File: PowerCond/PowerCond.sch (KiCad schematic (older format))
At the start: 42 parts, among them J1 Conn_01x02, J10 Conn_01x01, J11 Conn_01x01, J12 Conn_01x01, J2 Conn_01x02, J3 Conn_01x02, J4 Conn_01x02, J5 Conn_01x02, J6 Conn_01x02, J7 Conn_01x02, J8 Conn_01x02, J9 Conn_01x01, T1 Transformer_1P1Sdotted, T2 Transformer_1P1Sdotted, T3 Transformer_1P1Sdotted, T4 Transformer_1P1Sdotted

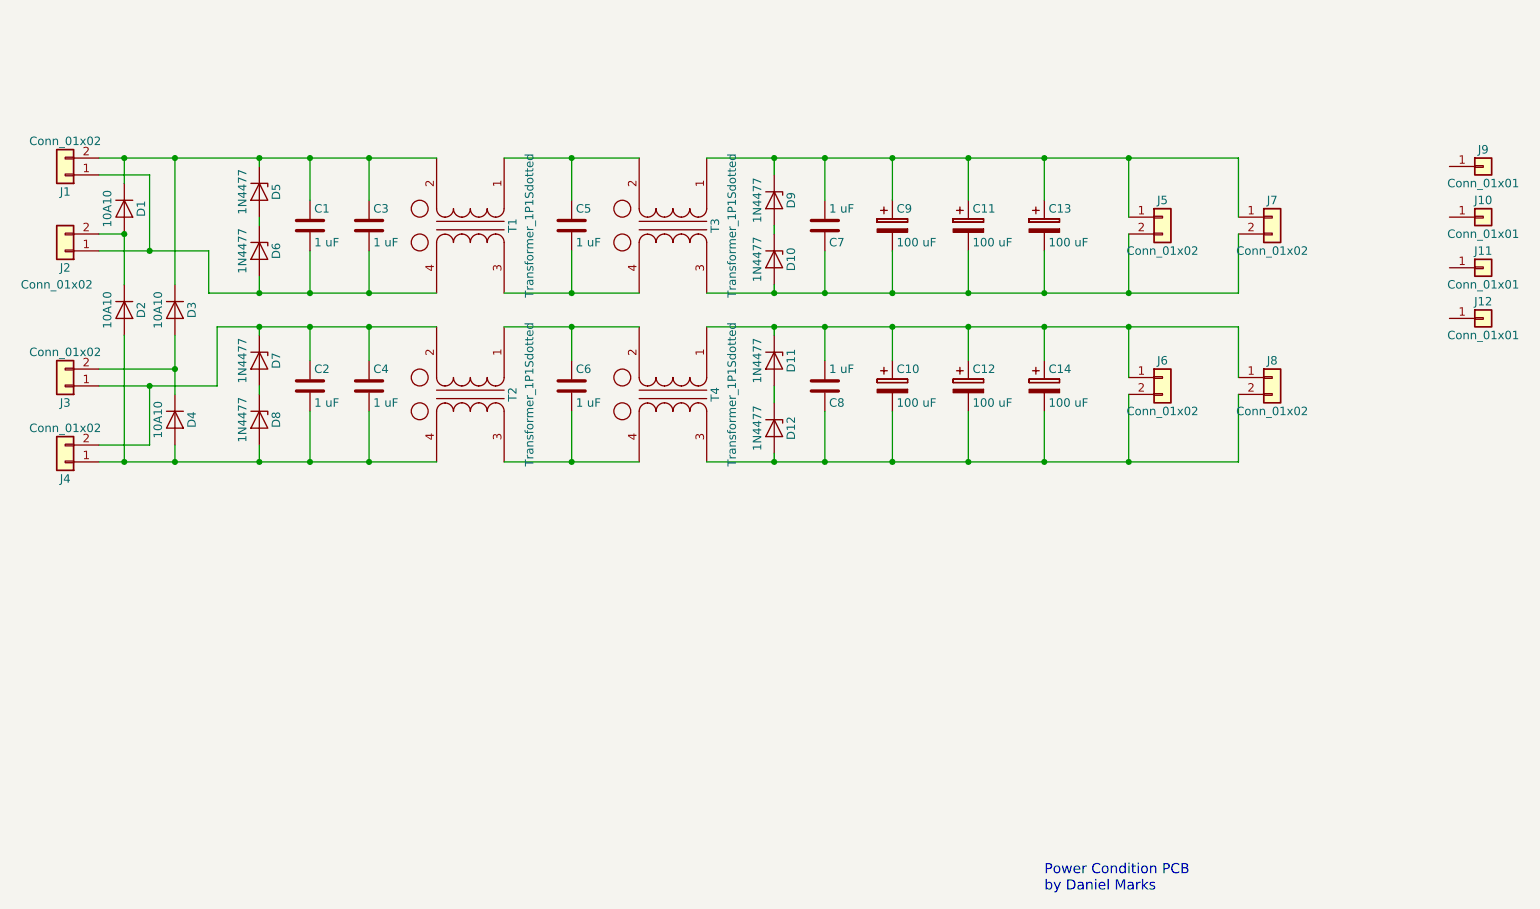
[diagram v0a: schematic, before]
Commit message: Added XLRtoBal
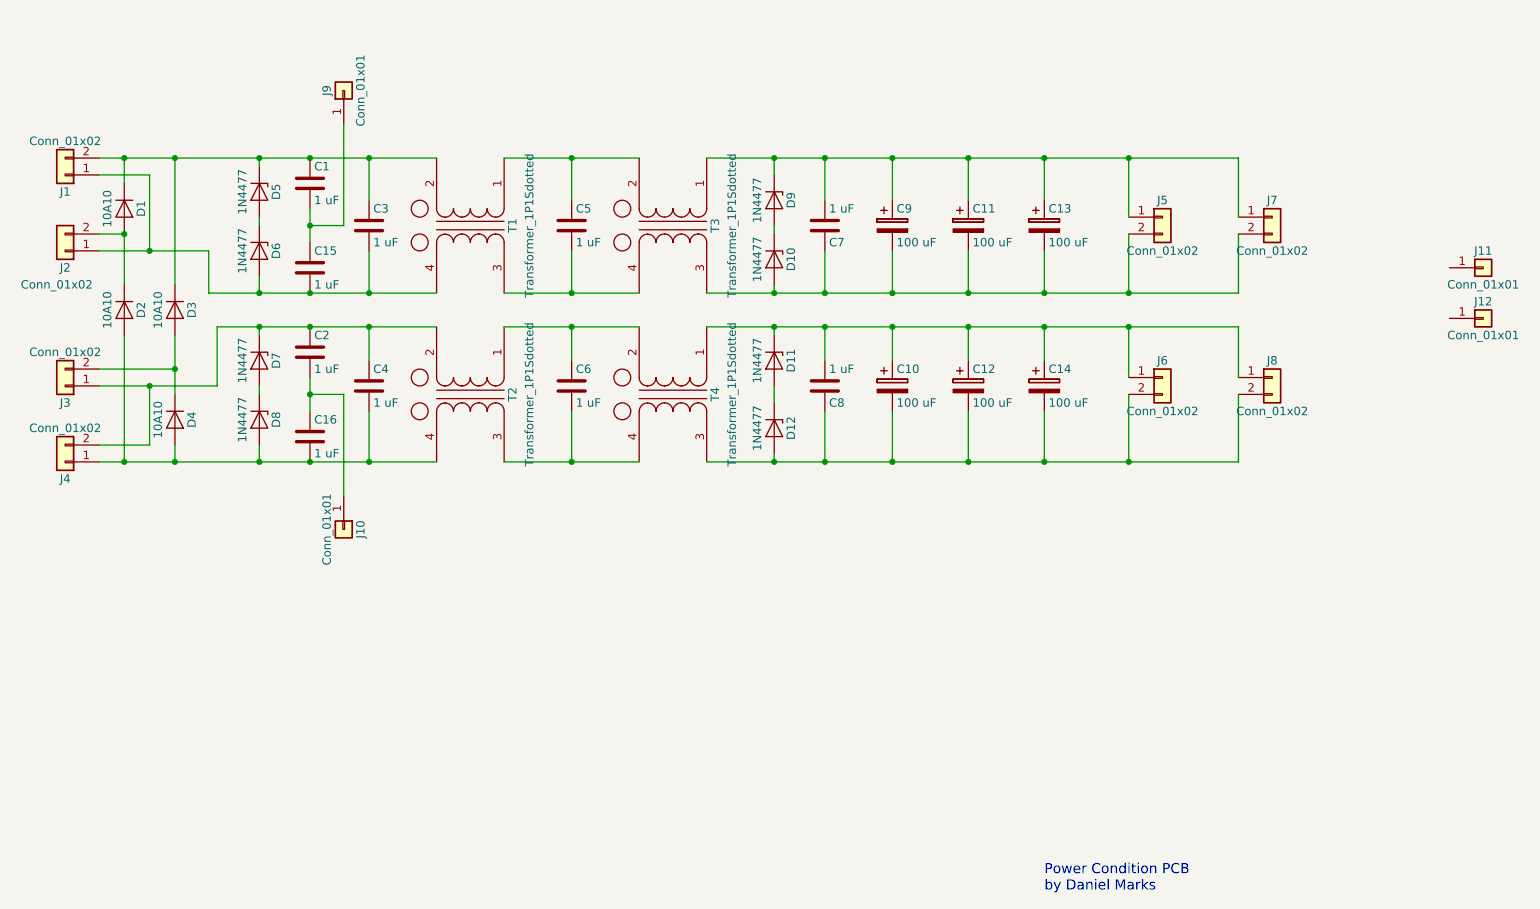
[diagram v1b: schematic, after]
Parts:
- added C15, C16: 1 uF, Capacitors_THT:C_Axial_L5.1mm_D3.1mm_P12.50mm_Horizontal, symbol C
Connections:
- net at J9.1 (Pin_1): now also C1.2, C15.1
- net at J10.1 (Pin_1): now also C2.2, C16.1
- net at C3.2, D6.2 (A), J1.1 (Pin_1)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: now also C15.2; no longer C1.2
- net at C4.2, D2.2 (A), D4.2 (A)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: now also C16.2; no longer C2.2
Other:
- moved on the sheet: C1, C2, J10, J9
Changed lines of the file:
@@
 L C C1
 U 1 1 5F3E50C0
-P 3200 3000
-F 0 "C1" H 3225 3100 50  0000 L CNN
-F 1 "1 uF" H 3225 2900 50  0000 L CNN
-F 2 "Capacitors_THT:C_Axial_L5.1mm_D3.1mm_P12.50mm_Horizontal" H 3238 2850 50  0001 C CNN
-F 3 "" H 3200 3000 50  0001 C CNN
-	1    3200 3000
-	1    0    0    -1
-$EndComp
-Wire Wire Line
-	3200 2850 3200 2600
+P 3200 2750
+F 0 "C1" H 3225 2850 50  0000 L CNN
+F 1 "1 uF" H 3225 2650 50  0000 L CNN
+F 2 "Capacitors_THT:C_Axial_L5.1mm_D3.1mm_P12.50mm_Horizontal" H 3238 2600 50  0001 C CNN
+F 3 "" H 3200 2750 50  0001 C CNN
+	1    3200 2750
+	1    0    0    -1
+$EndComp
+Wire Wire Line
+	3200 2600 3200 2600
 Connection ~ 3200 2600
-Wire Wire Line
-	3200 3150 3200 3400
 Connection ~ 3200 3400
 $Comp
@@
 L C C2
 U 1 1 5F3E52BA
-P 3200 3950
-F 0 "C2" H 3225 4050 50  0000 L CNN
-F 1 "1 uF" H 3225 3850 50  0000 L CNN
-F 2 "Capacitors_THT:C_Axial_L5.1mm_D3.1mm_P12.50mm_Horizontal" H 3238 3800 50  0001 C CNN
-F 3 "" H 3200 3950 50  0001 C CNN
-	1    3200 3950
-	1    0    0    -1
-$EndComp
-Wire Wire Line
-	3200 3800 3200 3600
+P 3200 3750
+F 0 "C2" H 3225 3850 50  0000 L CNN
+F 1 "1 uF" H 3225 3650 50  0000 L CNN
+F 2 "Capacitors_THT:C_Axial_L5.1mm_D3.1mm_P12.50mm_Horizontal" H 3238 3600 50  0001 C CNN
+F 3 "" H 3200 3750 50  0001 C CNN
+	1    3200 3750
+	1    0    0    -1
+$EndComp
+Wire Wire Line
+	3200 3600 3200 3600
 Connection ~ 3200 3600
-Wire Wire Line
-	3200 4100 3200 4400
 Connection ~ 3200 4400
 $Comp
@@
 L Conn_01x01 J9
 U 1 1 5F3C25A0
-P 10150 2650
-F 0 "J9" H 10150 2750 50  0000 C CNN
-F 1 "Conn_01x01" H 10150 2550 50  0000 C CNN
-F 2 "Connectors:1pin" H 10150 2650 50  0001 C CNN
-F 3 "" H 10150 2650 50  0001 C CNN
-	1    10150 2650
-	1    0    0    -1
+P 3400 2200
+F 0 "J9" H 3400 2300 50  0000 C CNN
+F 1 "Conn_01x01" H 3400 2100 50  0000 C CNN
+F 2 "Connectors:1pin" H 3400 2200 50  0001 C CNN
+F 3 "" H 3400 2200 50  0001 C CNN
+	1    3400 2200
+	0    -1   -1   0
 $EndComp
 $Comp
 L Conn_01x01 J10
 U 1 1 5F3C2707
-P 10150 2950
-F 0 "J10" H 10150 3050 50  0000 C CNN
-F 1 "Conn_01x01" H 10150 2850 50  0000 C CNN
-F 2 "Connectors:1pin" H 10150 2950 50  0001 C CNN
-F 3 "" H 10150 2950 50  0001 C CNN
-	1    10150 2950
-	1    0    0    -1
+P 3400 4800
+F 0 "J10" H 3400 4900 50  0000 C CNN
+F 1 "Conn_01x01" H 3400 4700 50  0000 C CNN
+F 2 "Connectors:1pin" H 3400 4800 50  0001 C CNN
+F 3 "" H 3400 4800 50  0001 C CNN
+	1    3400 4800
+	0    1    1    0
 $EndComp
 $Comp
@@
 	1    0    0    -1
 $EndComp
+$Comp
+L C C15
+U 1 1 5F3CBB39
+P 3200 3250
+F 0 "C15" H 3225 3350 50  0000 L CNN
+F 1 "1 uF" H 3225 3150 50  0000 L CNN
+F 2 "Capacitors_THT:C_Axial_L5.1mm_D3.1mm_P12.50mm_Horizontal" H 3238 3100 50  0001 C CNN
+F 3 "" H 3200 3250 50  0001 C CNN
+	1    3200 3250
+	1    0    0    -1
+$EndComp
+Wire Wire Line
+	3200 3100 3200 2900
+$Comp
+L C C16
+U 1 1 5F3CBDE8
+P 3200 4250
+F 0 "C16" H 3225 4350 50  0000 L CNN
+F 1 "1 uF" H 3225 4150 50  0000 L CNN
+F 2 "Capacitors_THT:C_Axial_L5.1mm_D3.1mm_P12.50mm_Horizontal" H 3238 4100 50  0001 C CNN
+F 3 "" H 3200 4250 50  0001 C CNN
+	1    3200 4250
+	1    0    0    -1
+$EndComp
+Wire Wire Line
+	3200 4100 3200 3900
+Wire Wire Line
+	3400 2400 3400 3000
+Wire Wire Line
+	3400 3000 3200 3000
+Connection ~ 3200 3000
+Wire Wire Line
+	3400 4600 3400 4000
+Wire Wire Line
+	3400 4000 3200 4000
+Connection ~ 3200 4000
 $EndSCHEMATC

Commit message: Added soft start circuit
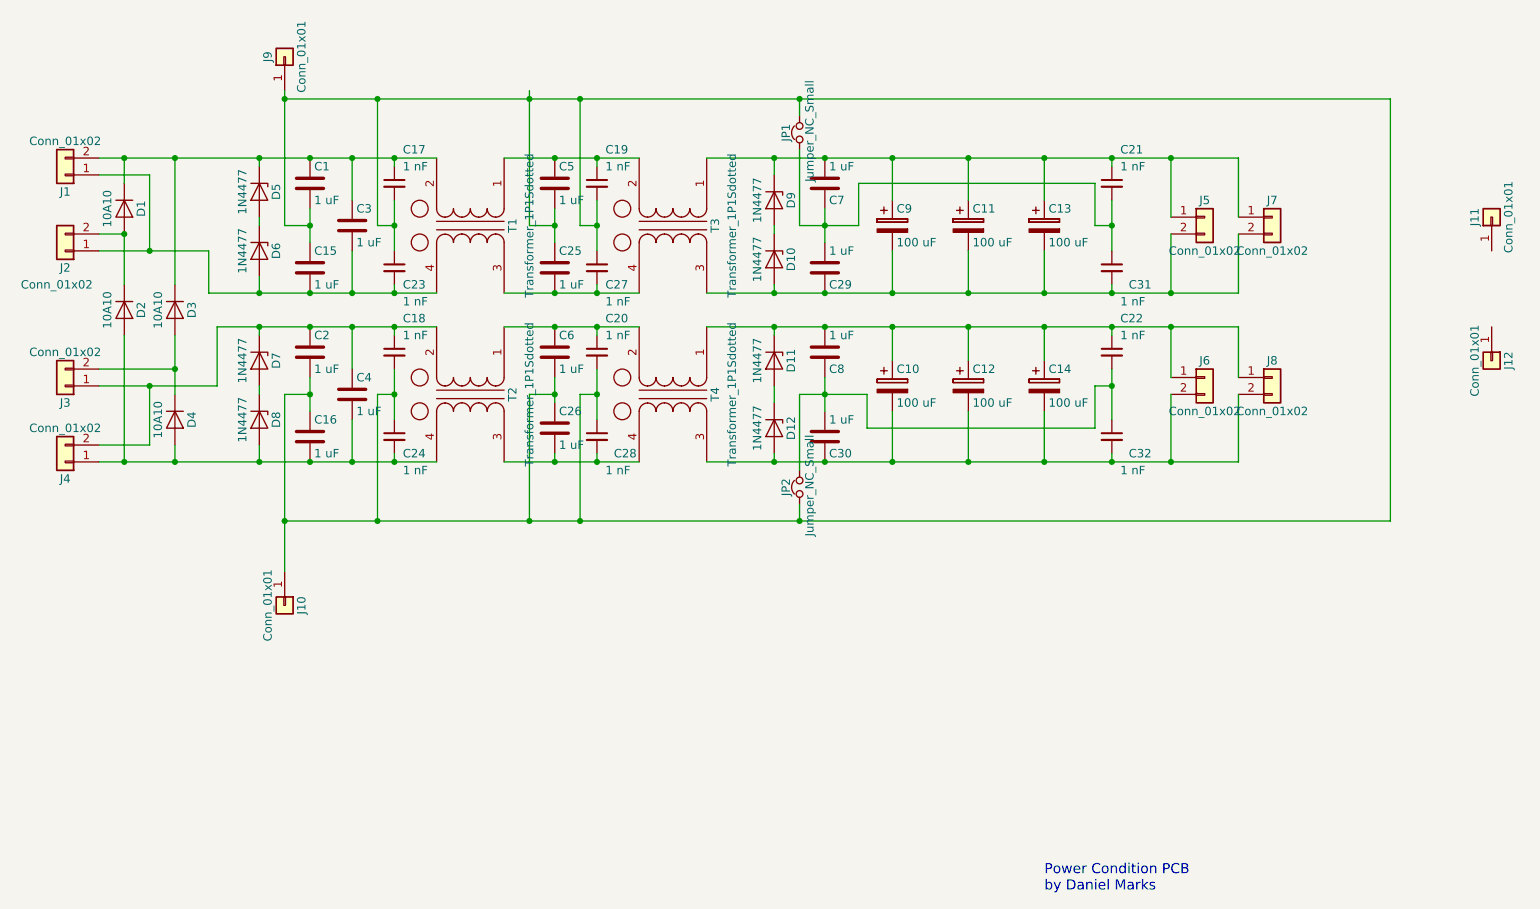
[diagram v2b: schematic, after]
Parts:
- added C17, C18, C19, C20, C21, C22, C23, C24, C27, C28, C31, C32: 1 nF, Capacitors_THT:C_Disc_D5.0mm_W2.5mm_P5.00mm, symbol C_Small
- added C25, C26, C29, C30: 1 uF, Capacitors_THT:C_Axial_L5.1mm_D3.1mm_P12.50mm_Horizontal, symbol C
- added JP1, JP2: Jumper_NC_Small, Pin_Headers:Pin_Header_Straight_1x02_Pitch2.54mm, symbol Jumper_NC_Small
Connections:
- net at C1.2, C15.1, J9.1 (Pin_1): now also C16.1, C2.2, C5.2, C6.2, J10.1 (Pin_1), C17.2, C18.2, C19.2, C20.2, C23.1, C24.1, C25.1, C26.1, C27.1, C28.1, JP1.2, JP2.1
- net at C15.2, C3.2, D6.2 (A)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: now also C23.2
- net at C16.2, C4.2, D2.2 (A)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: now also C24.2
- net at C5.1, T1.1 (AA), T3.2 (AB): now also C19.1
- net at C1.1, C3.1, D1.1 (K)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: now also C17.1
- net at T1.3 (SA), T3.4 (SB): now also C25.2, C27.2; no longer C5.2
- net at C2.1, C4.1, D7.1 (K)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: now also C18.1
- net at C6.1, T2.1 (AA), T4.2 (AB): now also C20.1
- net at T2.3 (SA), T4.4 (SB): now also C26.2, C28.2; no longer C6.2
- net at C11.1, C13.1, C7.2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: now also C21.1
- net at C11.2, C13.2, C9.2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: now also C29.1, C31.2; no longer C7.1
- net at C10.1, C12.1, C14.1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: now also C22.1
- net at C10.2, C12.2, C14.2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: now also C30.1, C32.2; no longer C8.1
- new net: C21.2, C29.2, C31.1, C7.1, JP1.1
- new net: C22.2, C30.2, C32.1, C8.1, JP2.2
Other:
- moved on the sheet: C3, C4, C5, C6, C7, C8, J10, J11, J12, J5, J6, J9

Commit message: Submitted to JLCPCB 2020-08-24
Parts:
- C1, C15, C16, C2, C25, C26, C29, C3, C30, C4, C5, C6, C7, C8: LCSC (none) -> C178471
- C10, C11, C12, C13, C14, C9: LCSC (none) -> C330940
- C17, C18, C20, C21, C22, C23, C24, C27, C28, C31, C32, T3: LCSC (none) -> C249151
- D1, D2, D3, D4: LCSC (none) -> C106904
- D10, D11, D12, D5, D6, D7, D8, D9: value 1N4477 -> 1N4755A; LCSC (none) -> C8043
- J1, J2, J3, J4, J5, J6, J7, J8: LCSC (none) -> C395849

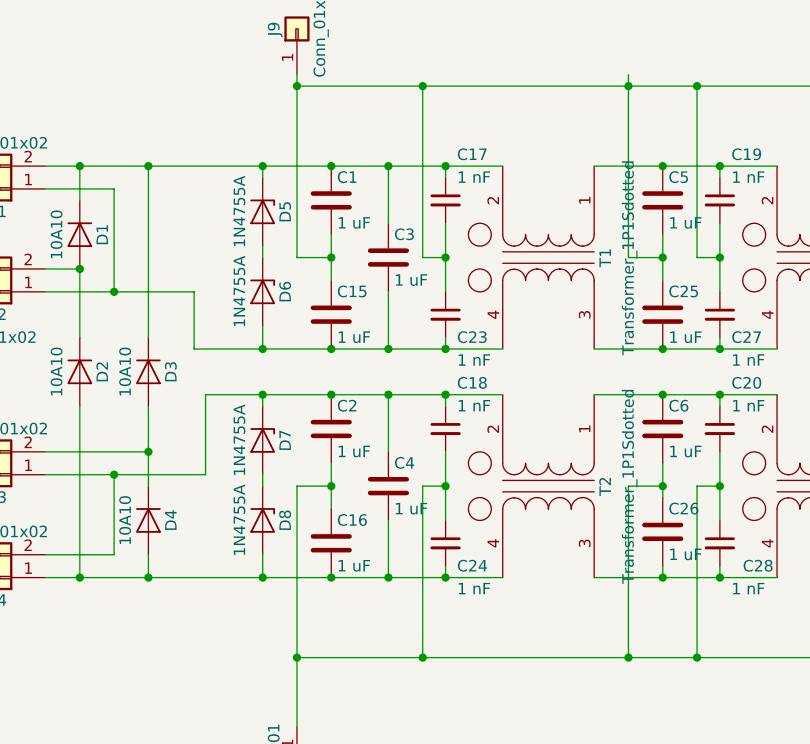
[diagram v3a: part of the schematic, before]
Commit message: Changed softstart and Poweramp to TO-220 transistors
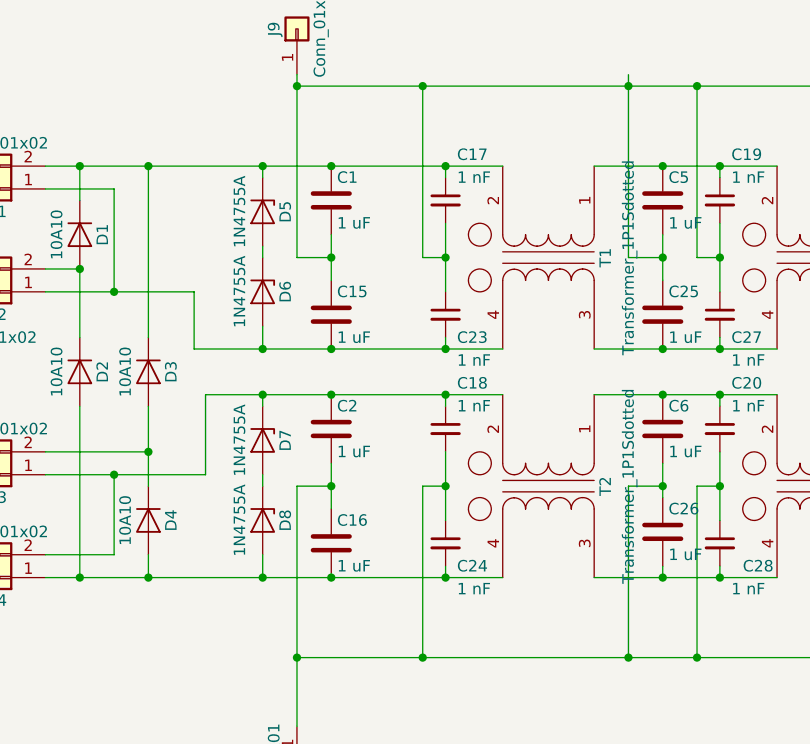
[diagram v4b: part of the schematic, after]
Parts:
- removed C3, C4: 1 uF, Capacitors_THT:C_Axial_L5.1mm_D3.1mm_P12.50mm_Horizontal, symbol C
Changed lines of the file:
@@
-$EndComp
-$Comp
-L C C3
-U 1 1 5F3E5214
-P 3450 3000
-F 0 "C3" H 3475 3100 50  0000 L CNN
-F 1 "1 uF" H 3475 2900 50  0000 L CNN
-F 2 "Capacitors_THT:C_Axial_L5.1mm_D3.1mm_P12.50mm_Horizontal" H 3488 2850 50  0001 C CNN
-F 3 "" H 3450 3000 50  0001 C CNN
-F 4 "C178471" H 3450 3000 60  0001 C CNN "LCSC"
-	1    3450 3000
-	1    0    0    -1
 $EndComp
 $Comp
@@
 F 4 "C178471" H 3200 3750 60  0001 C CNN "LCSC"
 	1    3200 3750
-	1    0    0    -1
-$EndComp
-$Comp
-L C C4
-U 1 1 5F3E5377
-P 3450 4000
-F 0 "C4" H 3475 4100 50  0000 L CNN
-F 1 "1 uF" H 3475 3900 50  0000 L CNN
-F 2 "Capacitors_THT:C_Axial_L5.1mm_D3.1mm_P12.50mm_Horizontal" H 3488 3850 50  0001 C CNN
-F 3 "" H 3450 4000 50  0001 C CNN
-F 4 "C178471" H 3450 4000 60  0001 C CNN "LCSC"
-	1    3450 4000
 	1    0    0    -1
 $EndComp
@@
 	3050 4000 3050 5050
 Wire Wire Line
-	3450 3850 3450 3600
-Connection ~ 3450 3600
-Wire Wire Line
-	3450 4150 3450 4400
-Connection ~ 3450 4400
-Wire Wire Line
 	3700 3650 3700 3600
 Connection ~ 3700 3600
@@
 	3050 2200 3050 3000
 Wire Wire Line
-	3450 2850 3450 2600
-Connection ~ 3450 2600
-Wire Wire Line
-	3450 3150 3450 3400
-Connection ~ 3450 3400
-Wire Wire Line
 	3700 2650 3700 2600

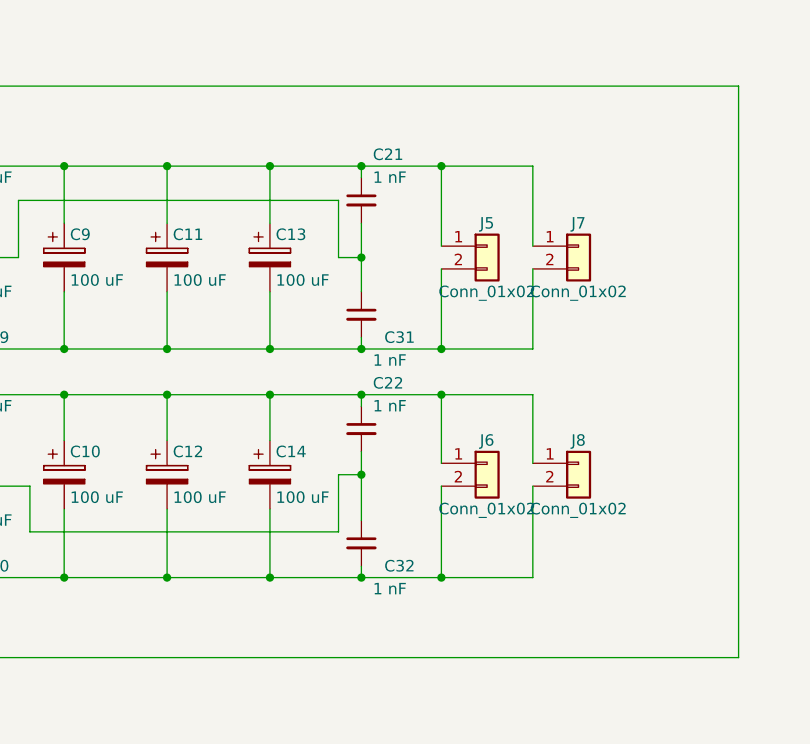
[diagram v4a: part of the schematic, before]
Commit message: Changed to 2N5551/2N5401 from BC546C/BC556C transistors
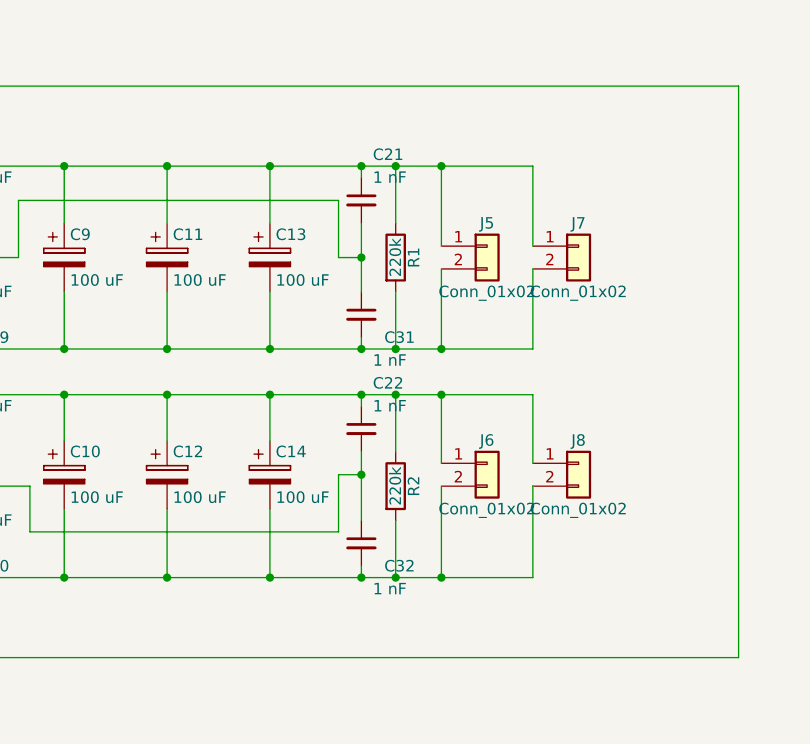
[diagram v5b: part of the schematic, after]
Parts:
- added R1, R2: 220k, Resistors_THT:R_Axial_DIN0309_L9.0mm_D3.2mm_P12.70mm_Horizontal, symbol R
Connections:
- net at C11.1, C13.1, C21.1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: now also R1.1
- net at C11.2, C13.2, C29.1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: now also R1.2
- net at C10.1, C12.1, C14.1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: now also R2.1
- net at C10.2, C12.2, C14.2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: now also R2.2
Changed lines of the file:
@@
 Connection ~ 7550 4400
 Connection ~ 7950 4400
+$Comp
+L R R1
+U 1 1 5F5F98B3
+P 8100 3000
+F 0 "R1" V 8180 3000 50  0000 C CNN
+F 1 "220k" V 8100 3000 50  0000 C CNN
+F 2 "Resistors_THT:R_Axial_DIN0309_L9.0mm_D3.2mm_P12.70mm_Horizontal" V 8030 3000 50  0001 C CNN
+F 3 "" H 8100 3000 50  0001 C CNN
+	1    8100 3000
+	1    0    0    -1
+$EndComp
+Wire Wire Line
+	8100 2850 8100 2600
+Connection ~ 8100 2600
+Wire Wire Line
+	8100 3150 8100 3400
+Connection ~ 8100 3400
+$Comp
+L R R2
+U 1 1 5F5FA14C
+P 8100 4000
+F 0 "R2" V 8180 4000 50  0000 C CNN
+F 1 "220k" V 8100 4000 50  0000 C CNN
+F 2 "Resistors_THT:R_Axial_DIN0309_L9.0mm_D3.2mm_P12.70mm_Horizontal" V 8030 4000 50  0001 C CNN
+F 3 "" H 8100 4000 50  0001 C CNN
+	1    8100 4000
+	1    0    0    -1
+$EndComp
+Wire Wire Line
+	8100 3850 8100 3600
+Connection ~ 8100 3600
+Wire Wire Line
+	8100 4150 8100 4400
+Connection ~ 8100 4400
 $EndSCHEMATC
